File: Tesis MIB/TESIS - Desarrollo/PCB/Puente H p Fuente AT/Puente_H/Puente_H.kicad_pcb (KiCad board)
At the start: 2 copper layers, 120 x 80 mm, 89 parts, among them J1 Vfb+, J10 PIN_+12V, J11 PIN_GND, J12 PIN_+5V, J13 Screw_Terminal_01x04, J14 Screw_Terminal_01x03, J2 Vfb-, J3 Screw_Terminal_01x02, J4 Screw_Terminal_01x02, J5 Vfb, J6 PB_ICout, J7 PA_ICout, J8 PB_BDin, J9 PA_BDin, Q1 BC547, Q2 BC547, Q3 BC337, Q4 IRF3205, Q5 IRF3205, Q6 IRF3205, Q7 IRF3205, Q8 BC547, Q9 BC547, T1 Transformer_1P_1S, U1 NA555P, U2 4N27, U3 4N27, U4 SG3525, U5 LM7805_TO220, U6 4N27, U7 4N27

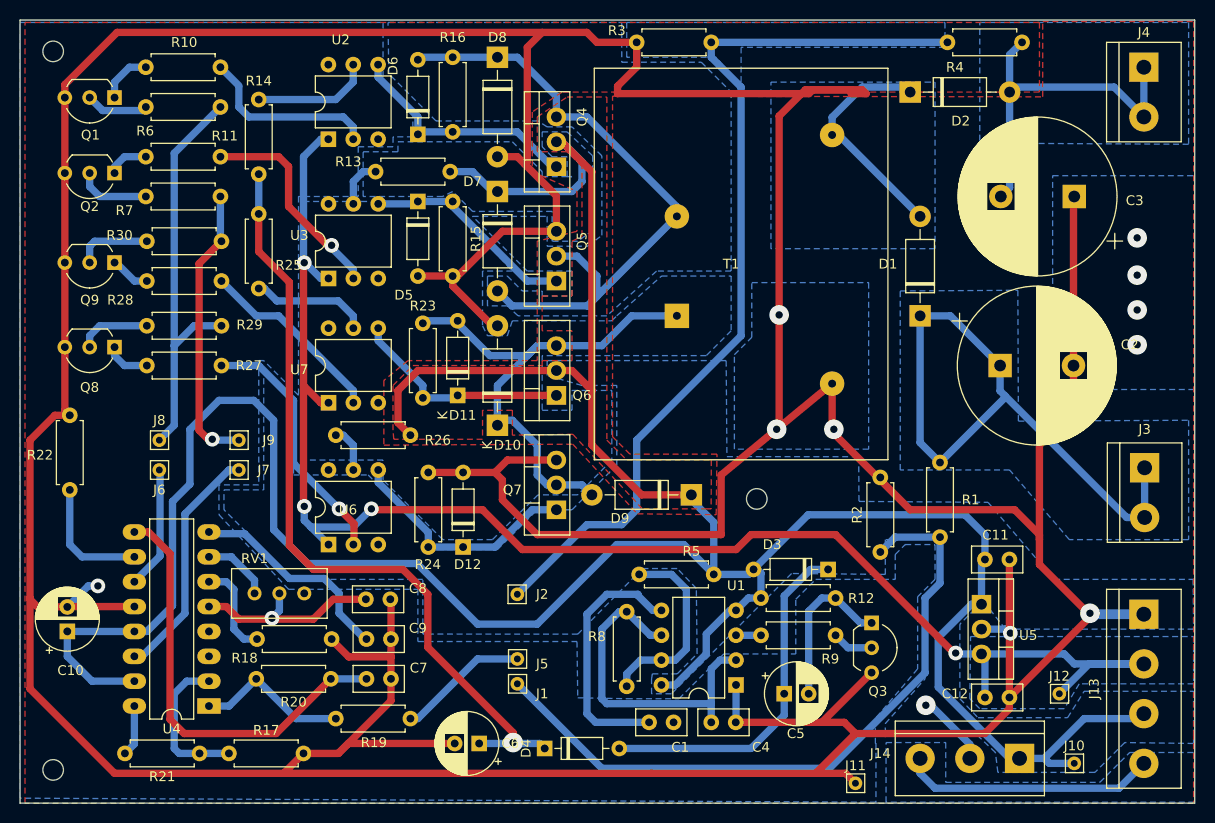
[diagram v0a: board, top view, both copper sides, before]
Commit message: Acualización del CAP2
Finalización de la 1ra parte del CAP2, redacción de titulos y subtitulos para esquematizar los CAP3 y CAP4, actualización de los indices de Contenidos, Tablas y Figuras y Referencias insertadas (hasta la 48).
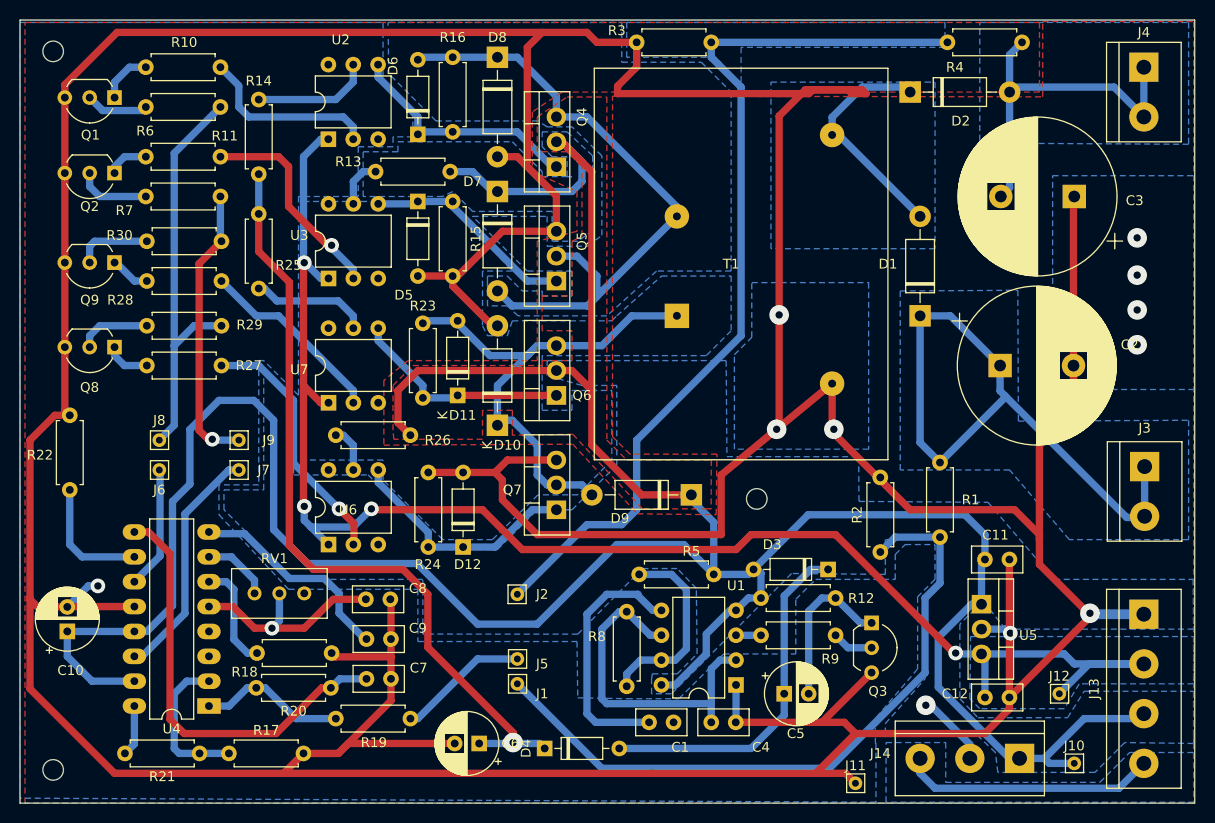
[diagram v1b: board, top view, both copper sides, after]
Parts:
- moved R18 1.43 mm to (95.8, 100.1)
- moved R20 0.92 mm to (103.3, 103.6)
- moved J3 0.12 mm to (186.4, 81.0)
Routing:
- net Net-(C8-Pad2): track 20.4 -> 22.3 mm
- net Net-(R18-Pad1): track 9.64 -> 10.9 mm
- net Net-(R19-Pad1): track 15.8 -> 15.0 mm
- net GND: track 624.1 -> 623.5 mm

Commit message: Actualiza CAP 2 parcial 2
Actualiza el documento de tesis con el CAP 2 casi finalizado, solo resto agregar "Simulaciones" y cierre final.
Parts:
- removed R17: 5k1, Resistor_THT:R_Axial_DIN0207_L6.3mm_D2.5mm_P7.62mm_Horizontal
- added RV2: 10k, Potentiometer_THT:Potentiometer_Bourns_3296W_Vertical, F.Cu at (99.1, 110.2)
- RV1: value R_Potentiometer -> 1k
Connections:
- net /+300v renamed /+Vat
- net /-300v renamed /-Vat
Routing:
- net Net-(U4-NI): track 15.5 -> 16.6 mm
- net GND: track 623.5 -> 624.1 mm

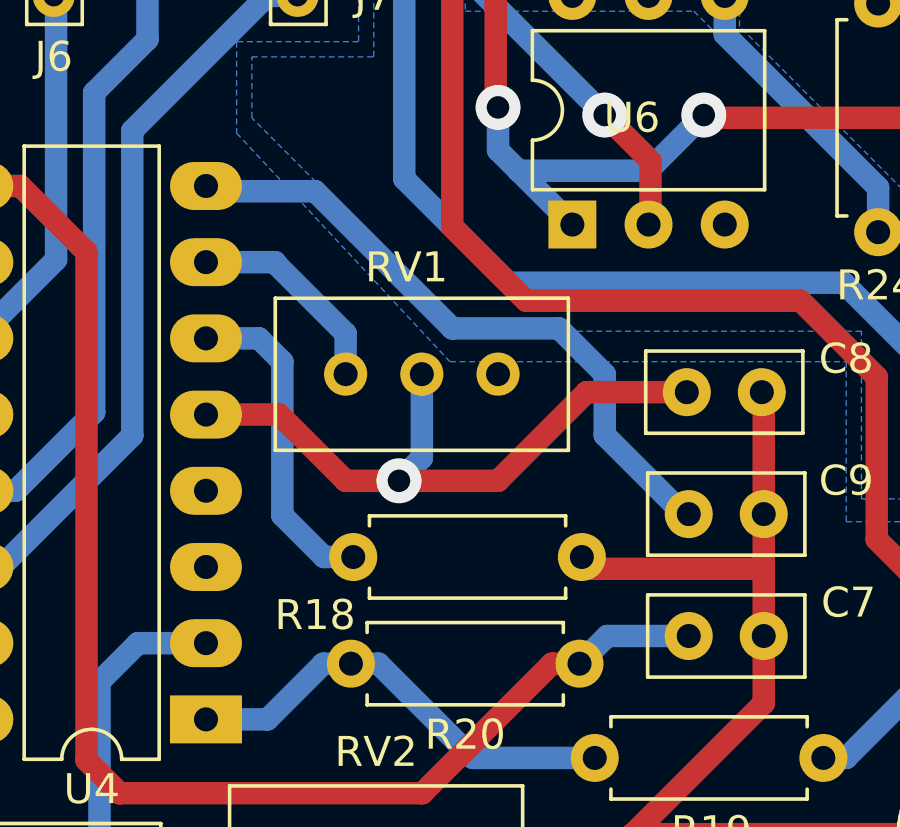
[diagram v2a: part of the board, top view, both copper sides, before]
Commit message: Actualiza Pruebas
Agrega planilla, gráficos y capturas del osciloscopio para el CAP3
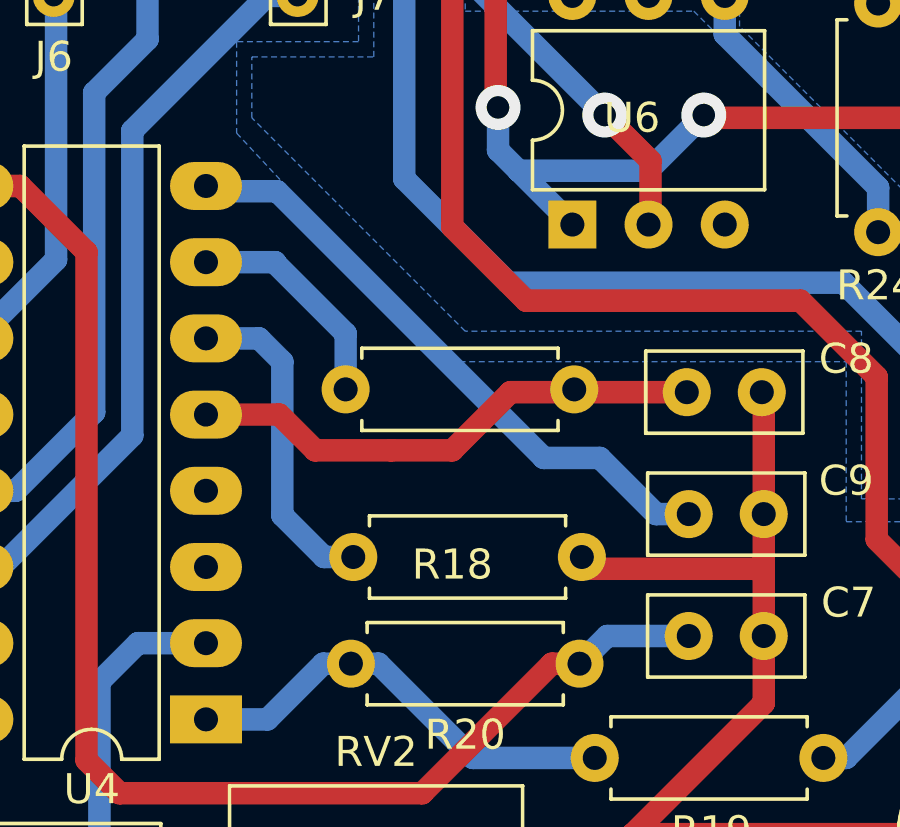
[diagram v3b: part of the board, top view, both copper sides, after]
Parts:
- removed RV1: 1k, Potentiometer_THT:Potentiometer_Bourns_3296W_Vertical
- added R17: 470, Resistor_THT:R_Axial_DIN0207_L6.3mm_D2.5mm_P7.62mm_Horizontal, F.Cu at (95.5, 94.5)
- C8: value 47nF -> 47nF (39nF)
- R18: value 27k -> 39k (37.8k)
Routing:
- net Net-(U4-CT): track 22.3 -> 17.3 mm, vias 1 -> 0
- net Net-(U4-SS): track 21.8 -> 20.6 mm
- net Net-(U4-DISCH): track 7.01 -> 7.52 mm
